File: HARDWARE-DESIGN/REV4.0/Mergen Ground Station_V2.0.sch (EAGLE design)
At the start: 87 parts, among them J2 CON-SD-CARD_MICROSD-2908-05, J4 U.FL, U13 L86, U15 AMS1117-5V, U16 AMS1117-3.3, X2 JST-XH-04-PIN-LONG-PAD, Y1 ABMM2-8.000MHZ-E2-T

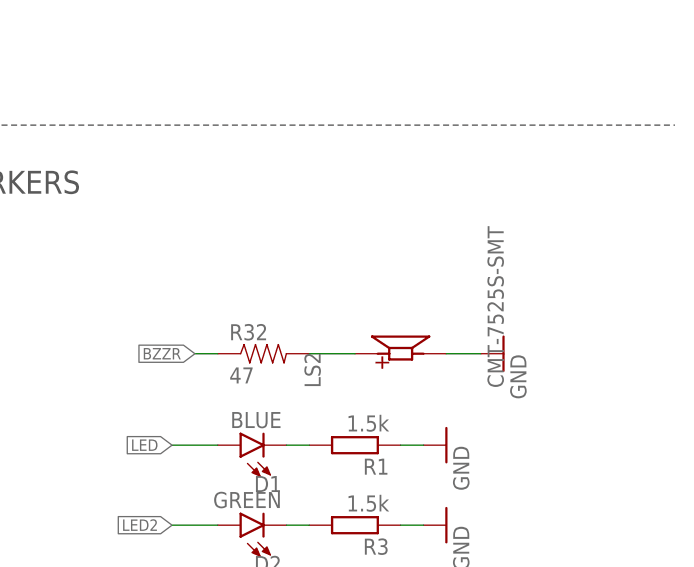
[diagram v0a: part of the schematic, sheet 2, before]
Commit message: Lora configuration connectors were added
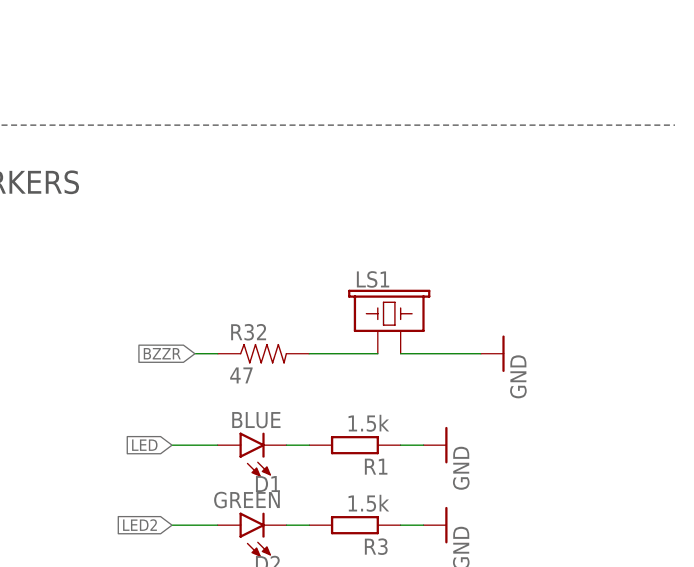
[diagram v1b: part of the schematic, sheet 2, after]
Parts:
- removed LS2: CMT-7525S-SMT, CMT-7525S-SMT:CMT-7525S-SMT
- added J1: (no value), SparkFun-Connectors:CONN_04
- added LS1: BUZZER-PTH, SparkFun-Electromechanical:BUZZER-PTH
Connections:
- net 5V: now also J1.4
- net GND: now also J1.1, LS1.2; no longer LS2.N
- net N$4: now also LS1.1; no longer LS2.P
- net RX2: now also J1.2
- net TX2: now also J1.3
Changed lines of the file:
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@@
 <setting verticaltext="up"/>
 </settings>
-<grid distance="100" unitdist="mil" unit="mil" style="lines" multiple="1" display="yes" altdistance="0.01" altunitdist="inch" altunit="mil"/>
+<grid distance="50" unitdist="mil" unit="mil" style="lines" multiple="1" display="yes" altdistance="0.01" altunitdist="inch" altunit="mil"/>
 <layers>
 <layer number="1" name="Top" color="4" fill="1" visible="no" active="no"/>
@@
 <part name="R3" library="rcl" library_urn="urn:adsk.eagle:library:334" deviceset="R-EU_" device="R0603" package3d_urn="urn:adsk.eagle:package:23555/3" value="1.5k"/>
 <part name="GND12" library="supply1" library_urn="urn:adsk.eagle:library:371" deviceset="GND" device=""/>
-<part name="LS2" library="CMT-7525S-SMT" deviceset="CMT-7525S-SMT" device=""/>
 <part name="U1" library="ELTASSAN" deviceset="MDBT42T-AT" device="">
 <attribute name="COMPONENT" value="MODULE BLUETOOTH BT4.2/5 nRF52805 SOC CHIP ANTENNA"/>
@@
 <part name="SUPPLY9" library="SparkFun-PowerSymbols" library_urn="urn:adsk.eagle:library:530" deviceset="5V" device=""/>
 <part name="P+3" library="supply1" library_urn="urn:adsk.eagle:library:371" deviceset="VCC" device="" value="8.4V"/>
+<part name="LS1" library="SparkFun-Electromechanical" library_urn="urn:adsk.eagle:library:516" deviceset="BUZZER" device="-PTH" package3d_urn="urn:adsk.eagle:package:38558/1"/>
+<part name="J1" library="SparkFun-Connectors" library_urn="urn:adsk.eagle:library:27162923" deviceset="CONN_04" device="" package3d_urn="urn:adsk.eagle:package:27162919/2"/>
+<part name="SUPPLY10" library="SparkFun-PowerSymbols" library_urn="urn:adsk.eagle:library:530" deviceset="5V" device=""/>
+<part name="GND14" library="supply1" library_urn="urn:adsk.eagle:library:371" deviceset="GND" device=""/>
 </parts>
 <sheets>
@@
 <attribute name="VALUE" x="254" y="26.67" size="1.778" layer="96" rot="R90"/>
 </instance>
-<instance part="LS2" gate="G$1" x="246.38" y="50.8" smashed="yes" rot="R90">
-<attribute name="NAME" x="237.488159375" y="46.989209375" size="1.77836875" layer="95" rot="R90"/>
-<attribute name="VALUE" x="257.8274" y="46.98418125" size="1.780709375" layer="96" rot="R90"/>
+<instance part="LS1" gate="G$1" x="243.84" y="53.34" smashed="yes">
+<attribute name="NAME" x="241.3" y="58.166" size="1.778" layer="95" font="vector"/>
 </instance>
 </instances>
@@
 </segment>
 <segment>
+<pinref part="LS1" gate="G$1" pin="2"/>
 <pinref part="GND49" gate="1" pin="GND"/>
-<wire x1="251.46" y1="50.8" x2="255.27" y2="50.8" width="0.1524" layer="91"/>
-<pinref part="LS2" gate="G$1" pin="N"/>
+<wire x1="246.38" y1="50.8" x2="255.27" y2="50.8" width="0.1524" layer="91"/>
 </segment>
 </net>
@@
 </segment>
 </net>
-<net name="N$4" class="0">
-<segment>
-<pinref part="R32" gate="G$1" pin="2"/>
-<wire x1="236.22" y1="50.8" x2="241.3" y2="50.8" width="0.1524" layer="91"/>
-<pinref part="LS2" gate="G$1" pin="P"/>
-</segment>
-</net>
 <net name="UART-PD" class="0">
 <segment>
@@
 <wire x1="38.1" y1="111.76" x2="33.02" y2="111.76" width="0.1524" layer="91"/>
 <label x="33.02" y="111.76" size="1.27" layer="95" rot="R180" xref="yes"/>
+</segment>
+</net>
+<net name="N$4" class="0">
+<segment>
+<pinref part="R32" gate="G$1" pin="2"/>
+<pinref part="LS1" gate="G$1" pin="1"/>
+<wire x1="236.22" y1="50.8" x2="243.84" y2="50.8" width="0.1524" layer="91"/>
 </segment>
 </net>
@@
 <attribute name="SHEET" x="199.39" y="5.08" size="2.54" layer="94" font="vector"/>
 </instance>
+<instance part="J1" gate="G$1" x="59.69" y="114.3" smashed="yes">
+<attribute name="VALUE" x="54.61" y="106.934" size="1.778" layer="96" font="vector"/>
+<attribute name="NAME" x="54.61" y="122.428" size="1.778" layer="95" font="vector"/>
+</instance>
+<instance part="SUPPLY10" gate="G$1" x="69.85" y="121.92" smashed="yes">
+<attribute name="VALUE" x="69.85" y="124.714" size="1.778" layer="96" align="bottom-center"/>
+</instance>
+<instance part="GND14" gate="1" x="69.85" y="106.68" smashed="yes">
+<attribute name="VALUE" x="64.77" y="104.14" size="1.778" layer="96"/>
+</instance>
 </instances>
 <busses>
@@
 <junction x="113.03" y="91.44"/>
 </segment>
+<segment>
+<pinref part="J1" gate="G$1" pin="1"/>
+<pinref part="GND14" gate="1" pin="GND"/>
+<wire x1="64.77" y1="111.76" x2="69.85" y2="111.76" width="0.1524" layer="91"/>
+<wire x1="69.85" y1="111.76" x2="69.85" y2="109.22" width="0.1524" layer="91"/>
+</segment>
 </net>
 <net name="M0" class="0">
@@
 <junction x="151.13" y="118.11"/>
 </segment>
+<segment>
+<pinref part="J1" gate="G$1" pin="4"/>
+<pinref part="SUPPLY10" gate="G$1" pin="5V"/>
+<wire x1="64.77" y1="119.38" x2="69.85" y2="119.38" width="0.1524" layer="91"/>
+<wire x1="69.85" y1="119.38" x2="69.85" y2="121.92" width="0.1524" layer="91"/>
+</segment>
 </net>
 <net name="N$27" class="0">
@@
 <label x="90.17" y="114.3" size="1.27" layer="95" rot="R180" xref="yes"/>
 </segment>
+<segment>
+<pinref part="J1" gate="G$1" pin="3"/>
+<wire x1="64.77" y1="116.84" x2="69.85" y2="116.84" width="0.1524" layer="91"/>
+<label x="69.85" y="116.84" size="1.27" layer="95" xref="yes"/>
+</segment>
 </net>
 <net name="RX2" class="0">
@@
 <label x="90.17" y="116.84" size="1.27" layer="95" rot="R180" xref="yes"/>
 </segment>
-</net>
+<segment>
+<pinref part="J1" gate="G$1" pin="2"/>
+<wire x1="64.77" y1="114.3" x2="69.85" y2="114.3" width="0.1524" layer="91"/>
+<label x="69.85" y="114.3" size="1.27" layer="95" xref="yes"/>
+</segment>
+</net>
